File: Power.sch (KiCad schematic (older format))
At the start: 0 parts

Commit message: Added power, touch, and motor controller
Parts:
- added C401, C409, C411: 10uF, Capacitors_SMD:C_0805, symbol C
- added C402: 1uf, Capacitors_SMD:C_0603, symbol C
- added C404, C410: 1uF, Capacitors_SMD:C_0603, symbol C
- added C406: 4.7uF, Capacitors_SMD:C_0603, symbol C
- added D401: 1N5819, Diodes_SMD:D_SOD-123, symbol D_Schottky
- added D403, D404: LED, LEDs:LED_0805, symbol LED
- added J?: Screw_Terminal_01x02, symbol Screw_Terminal_01x02
- added L401: 10uH, Inductors_SMD:L_0603, symbol L
- added L403: 2.2uH, Inductors_SMD:L_0603, symbol L
- added R401: 3.01K, Resistors_SMD:R_0603, symbol R
- added R402: 1K, Resistors_SMD:R_0603, symbol R
- added R405: 10K, Resistors_SMD:R_0603, symbol R
- added R406: 3.57K, Resistors_SMD:R_0603, symbol R
- added R407, R409: 1.5K, Resistors_SMD:R_0603, symbol R
- added R408: 2.94K, Resistors_SMD:R_0603, symbol R
- added R410: 4.32K, Resistors_SMD:R_0603, symbol R
- added R411: 56.2K, Resistors_SMD:R_0603, symbol R
- added U401: AP3012, TO_SOT_Packages_SMD:SOT-23-5, symbol AP3012
- added U403: TPS6223x, Custom:UFDFN-6-1.5x1.05mm_Pitch0.5mm, symbol TPS6223x
- added U405: BQ2423, Housings_DFN_QFN:QFN-16-1EP_3x3mm_Pitch0.5mm_ThermalVias, symbol BQ2423
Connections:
- new net: L403.2, U403.2 (SW)
- new net: R405.2, U405.1 (TS)
- new net: C409.1, J?.2 (Pin_2), U405.2 (BAT), U405.3 (BAT)
- new net: R408.1, U405.12 (ILIM)
- new net: R411.1, U405.14 (TMR)
- new net: R406.1, U405.15 (ITERM)
- new net: R410.1, U405.16 (ISET)
- new net: D403.1 (K), U405.7 (~PGOOD)
- new net: D404.1 (K), U405.9 (~CHG)
- new net: D403.2 (A), R407.2
- new net: D404.2 (A), R409.2
- new net: R401.2, R402.1, U401.3 (FB)
- new net: D401.2 (A), L401.1, U401.1 (SW)
- new net 3V3: C406.1, L403.1, U403.6 (FB)
- new net 3V7: C401.1, C402.1, C411.2, L401.2, R407.1, R409.1, U401.4 (SHDN), U401.5 (VIN), U403.3 (VIN), U403.5 (EN), U405.10 (OUT), U405.11 (OUT), U405.5 (EN2)
- new net 5V: C404.1, D401.1 (K), R401.1
- new net GND: C401.2, C402.2, C404.2, C406.2, C409.2, C410.2, C411.1, J?.1 (Pin_1), R402.2, R405.1, R406.2, R408.2, R410.2, R411.2, U401.2 (GND), U403.1 (MODE), U403.4 (GND), U405.4 (~CE), U405.6 (EN1), U405.8 (VSS)
- new net USB5V: C410.1, U405.13 (IN)
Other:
- note added: "3V3 Regulator"
- note added: "Battery Management"
- note added: "Boost Converter, 5V"

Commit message: Adding IR Sensor
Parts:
- gave numbers to parts that had none: 1
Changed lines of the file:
@@
 	1300 900  1300 1050
 $Comp
-L GND #PWR054
+L GND #PWR037
 U 1 1 59FB2340
 P 925 1325
-F 0 "#PWR054" H 925 1075 50  0001 C CNN
+F 0 "#PWR037" H 925 1075 50  0001 C CNN
 F 1 "GND" H 925 1175 50  0000 C CNN
 F 2 "" H 925 1325 50  0001 C CNN
@@
 	925  1200 925  1325
 $Comp
-L GND #PWR055
+L GND #PWR038
 U 1 1 59FB2347
 P 2600 1300
-F 0 "#PWR055" H 2600 1050 50  0001 C CNN
+F 0 "#PWR038" H 2600 1050 50  0001 C CNN
 F 1 "GND" H 2600 1150 50  0000 C CNN
 F 2 "" H 2600 1300 50  0001 C CNN
@@
 	2600 1300 2600 1200
 $Comp
-L GND #PWR056
+L GND #PWR039
 U 1 1 59FB234E
 P 3275 1300
-F 0 "#PWR056" H 3275 1050 50  0001 C CNN
+F 0 "#PWR039" H 3275 1050 50  0001 C CNN
 F 1 "GND" H 3275 1150 50  0000 C CNN
 F 2 "" H 3275 1300 50  0001 C CNN
@@
 $EndComp
 $Comp
-L GND #PWR057
+L GND #PWR040
 U 1 1 59FB392A
 P 8700 2425
-F 0 "#PWR057" H 8700 2175 50  0001 C CNN
+F 0 "#PWR040" H 8700 2175 50  0001 C CNN
 F 1 "GND" H 8700 2275 50  0000 C CNN
 F 2 "" H 8700 2425 50  0001 C CNN
@@
 $EndComp
 $Comp
-L GND #PWR058
+L GND #PWR041
 U 1 1 59FB394B
 P 8650 3175
-F 0 "#PWR058" H 8650 2925 50  0001 C CNN
+F 0 "#PWR041" H 8650 2925 50  0001 C CNN
 F 1 "GND" H 8650 3025 50  0000 C CNN
 F 2 "" H 8650 3175 50  0001 C CNN
@@
 $EndComp
 $Comp
-L GND #PWR059
+L GND #PWR042
 U 1 1 59FB396D
 P 9650 3375
-F 0 "#PWR059" H 9650 3125 50  0001 C CNN
+F 0 "#PWR042" H 9650 3125 50  0001 C CNN
 F 1 "GND" H 9650 3225 50  0000 C CNN
 F 2 "" H 9650 3375 50  0001 C CNN
@@
 $EndComp
 $Comp
-L GND #PWR060
+L GND #PWR043
 U 1 1 59FB397A
 P 10750 2475
-F 0 "#PWR060" H 10750 2225 50  0001 C CNN
+F 0 "#PWR043" H 10750 2225 50  0001 C CNN
 F 1 "GND" H 10750 2325 50  0000 C CNN
 F 2 "" H 10750 2475 50  0001 C CNN
@@
 $EndComp
 $Comp
-L GND #PWR061
+L GND #PWR044
 U 1 1 59FB3987
 P 10550 1475
-F 0 "#PWR061" H 10550 1225 50  0001 C CNN
+F 0 "#PWR044" H 10550 1225 50  0001 C CNN
 F 1 "GND" H 10550 1325 50  0000 C CNN
 F 2 "" H 10550 1475 50  0001 C CNN
@@
 Connection ~ 2975 2575
 $Comp
-L GND #PWR062
+L GND #PWR045
 U 1 1 59FB4920
 P 1925 3825
-F 0 "#PWR062" H 1925 3575 50  0001 C CNN
+F 0 "#PWR045" H 1925 3575 50  0001 C CNN
 F 1 "GND" H 1925 3675 50  0000 C CNN
 F 2 "" H 1925 3825 50  0001 C CNN
@@
 $EndComp
 $Comp
-L Screw_Terminal_01x02 J?
+L Screw_Terminal_01x02 J2
 U 1 1 5AA4D271
 P 8150 2925
-F 0 "J?" H 8150 3025 50  0000 C CNN
+F 0 "J2" H 8150 3025 50  0000 C CNN
 F 1 "Screw_Terminal_01x02" H 8150 2725 50  0000 C CNN
 F 2 "" H 8150 2925 50  0001 C CNN

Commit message: Finished Schematic
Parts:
- removed C402: 1uf, Capacitors_SMD:C_0603, symbol C
- removed C404: 1uF, Capacitors_SMD:C_0603, symbol C
- removed D401: 1N5819, Diodes_SMD:D_SOD-123, symbol D_Schottky
- removed L401: 10uH, Inductors_SMD:L_0603, symbol L
- removed R401: 3.01K, Resistors_SMD:R_0603, symbol R
- removed R402: 1K, Resistors_SMD:R_0603, symbol R
- removed U401: AP3012, TO_SOT_Packages_SMD:SOT-23-5, symbol AP3012
- added D? (x2): R_LED_3V3, symbol LED
- added R? (x2): 47, symbol R
- D403: value LED -> R_LED_PGOOD
- D404: value LED -> R_LED_CHG
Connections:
- net GND: now also D?.1 (K), D?.1 (K)
- net USB5V: now also R?.1
- net 3V3 renamed +3V3
- net +3V3: now also R?.1
- new net: D?.2 (A), R?.2 (x2)
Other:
- note added: "Power Indicating LEDs"
- note removed: "Boost Converter, 5V"
- moved on the sheet: C401, C406, C409, C410, C411, D403, D404, J2, L403, R405, R406, R407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

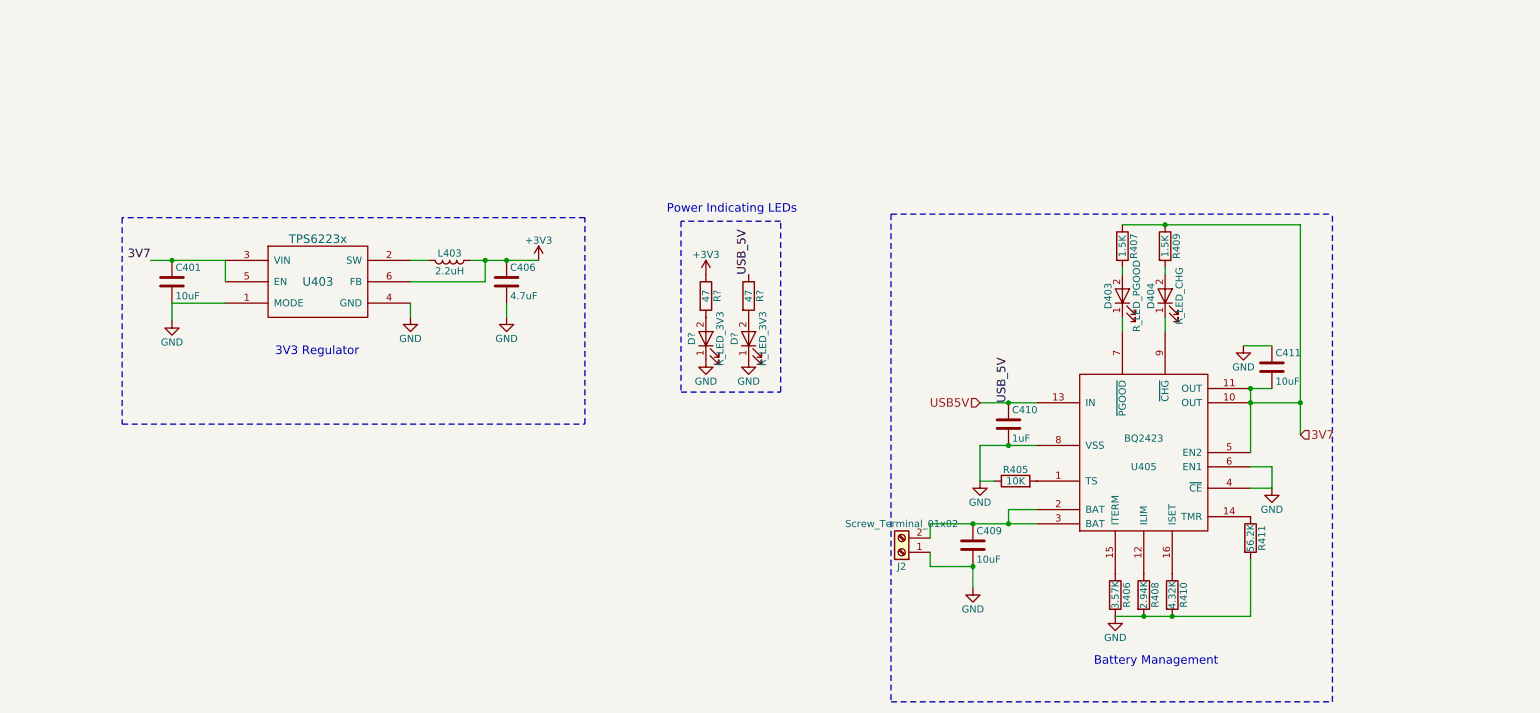
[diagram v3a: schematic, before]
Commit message: Started associating footprints
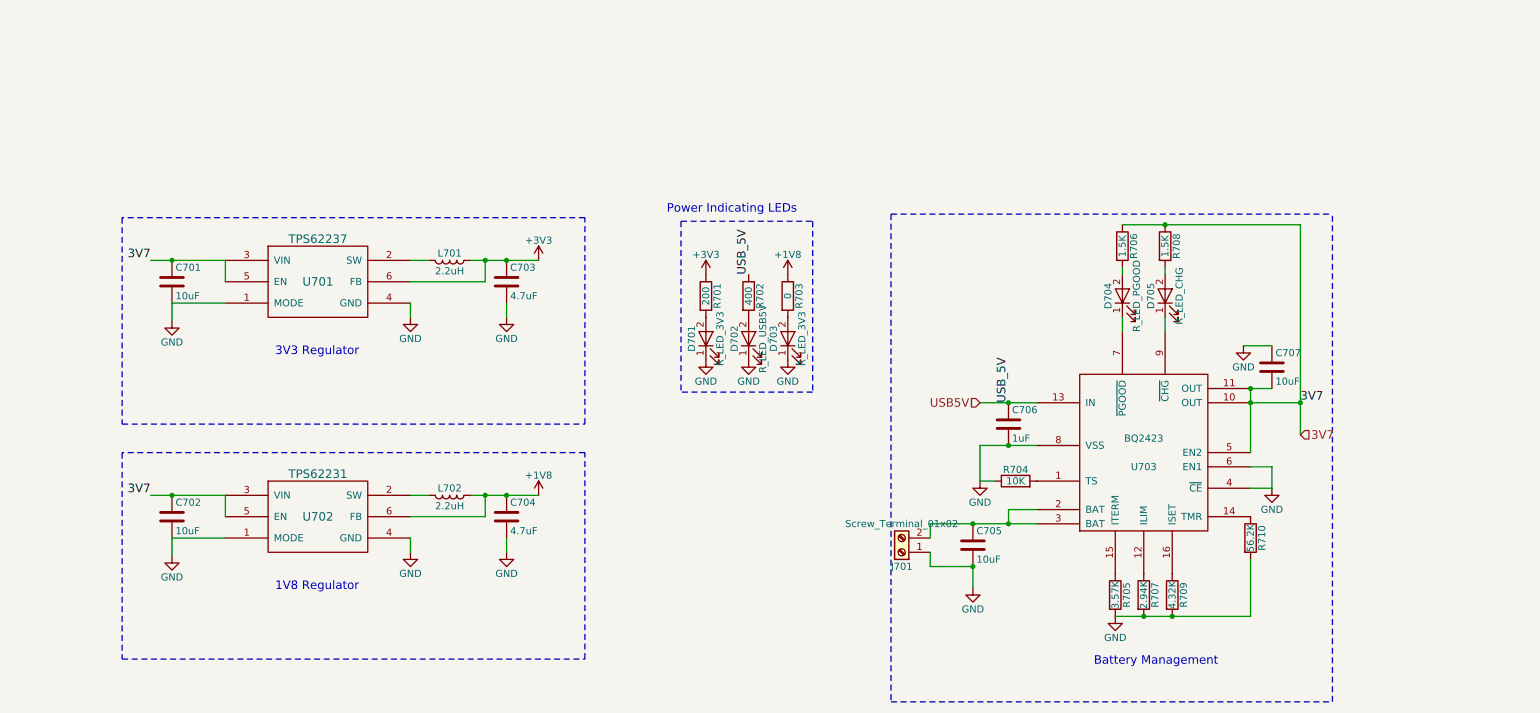
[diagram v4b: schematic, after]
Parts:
- added C702: 10uF, Capacitors_SMD:C_0603, symbol C
- added C704: 4.7uF, Capacitors_SMD:C_0603, symbol C
- added D703: R_LED_3V3, LEDs:LED_0805, symbol LED
- added L702: 2.2uH, Inductors_SMD:L_0603, symbol L
- added R703: 0, symbol R
- added U702: TPS62231, Custom:UFDFN-6-1.5x1.05mm_Pitch0.5mm, symbol TPS6223x
- C701: renamed from C401; footprint Capacitors_SMD:C_0805 -> Capacitors_SMD:C_0603
- C705: renamed from C409; footprint Capacitors_SMD:C_0805 -> Capacitors_SMD:C_0603
- C707: renamed from C411; footprint Capacitors_SMD:C_0805 -> Capacitors_SMD:C_0603
- D701: renamed from D?; footprint (none) -> LEDs:LED_0805
- D702: renamed from D?; value R_LED_3V3 -> R_LED_USB5V; footprint (none) -> LEDs:LED_0805
- R701: renamed from R?; value 47 -> 200
- R702: renamed from R?; value 47 -> 400
- U701: renamed from U403; value TPS6223x -> TPS62237
- renumbered C406 to C703, C410 to C706, D403 to D704, D404 to D705, J2 to J701, L403 to L701, R405 to R704, R406 to R705, R407 to R706, R408 to R707, R409 to R708, R410 to R709, R411 to R710, U405 to U703
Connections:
- net 3V7: now also C702.1, U702.3 (VIN), U702.5 (EN)
- net GND: now also C702.2, C704.2, D703.1 (K), U702.1 (MODE), U702.4 (GND)
- new net: D703.2 (A), R703.2
- new net: L702.2, U702.2 (SW)
- new net +1V8: C704.1, L702.1, R703.1, U702.6 (FB)
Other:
- note added: "1V8 Regulator"
